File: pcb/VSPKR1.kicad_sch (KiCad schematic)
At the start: 17 parts, among them J1 USB_C_Receptacle_USB2.0_14P, SW1 RESET, SW2 BOOT, U1 ESP32-S3-WROOM-1, U2 AMS1117-3.3

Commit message: added speaker stuffs
but i havent actually connected it to esp32
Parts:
- added C10, C7: 0.1uF, symbol Device:C
- added C6, C9: 2.2uF, symbol Device:C
- added C8: 1uF, symbol Device:C
- added R7: 1K, symbol Device:R
- added R8: 10K, symbol Device:R
- added SW3: SW_SPDT, symbol Switch:SW_SPDT
- added U3: PCM5102A, Package_SO:TSSOP-20_4.4x6.5mm_P0.65mm, symbol Audio:PCM5102A
- added U4: PAM8403D, Package_SO:SOIC-16_3.9x9.9mm_P1.27mm, symbol Amplifier_Audio:PAM8403D
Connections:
- net +3V3: now also C7.2, SW3.3 (C), U3.1 (CPVDD), U3.17 (XSMT), U3.20 (DVDD), U3.8 (AVDD)
- net +5V: now also U4.13 (PVDD), U4.4 (PVDD), U4.6 (VDD)
- net GND: now also C10.2, C9.2, R8.2, SW3.1 (A), U3.10 (DEMP), U3.11 (FLT), U3.12 (SCK), U3.16 (FMT), U3.19 (DGND), U3.3 (CPGND), U3.9 (AGND), U4.11 (GND), U4.15 (PGND), U4.2 (PGND)
- net SCK: no longer U1.15 (IO3)
- net WS: now also U3.15 (LRCK)
- net DOUT: now reaches U1.4 (IO4)
- net DOUT: now also U3.14 (DIN)
- net at U1.5 (IO5): now also R7.2
- new net: C10.1, U4.8 (VREF)
- new net: SW3.2 (B), U4.5 (~{MUTE})
- new net: C8.1, U3.18 (LDOO)
- new net: C6.1, U3.2 (CAPP)
- new net: C6.2, U3.4 (CAPM)
- new net: C7.1, U3.5 (VNEG)
- new net: C8.2, C9.1
- new net BCK: U1.15 (IO3), U3.13 (BCK)
- new net LEFT-CHANNEL-OUT: U3.6 (OUTL), U4.7 (INL)
- new net RIGHT-CHANNEL-OUT: U3.7 (OUTR), U4.10 (INR)
- new net SHND: R7.1, R8.1, U4.12 (~{SHDN})
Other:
- note added: "5V -> 3.3V Step Down"
- note added: "Mic"
- note added: "Microphone! No data collection here."
- note added: "Power Source"
- note added: "Sound"
- note removed: "Mic / Sound"
- moved on the sheet: C1, C2, J1, R1, R2, U2

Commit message: pcb time!!111!!!!1!
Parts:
- removed SW3: SW_SPDT, symbol Switch:SW_SPDT
- added C11: 22uF, Capacitor_SMD:C_0805_2012Metric_Pad1.18x1.45mm_HandSolder, symbol Device:C
- added C12: 100nF, Capacitor_SMD:C_0805_2012Metric_Pad1.18x1.45mm_HandSolder, symbol Device:C
- added J2, J3: Screw_Terminal_01x02, TerminalBlock_Phoenix:TerminalBlock_Phoenix_MKDS-1,5-2_1x02_P5.00mm_Horizontal, symbol Connector:Screw_Terminal_01x02
- C1, C10, C2, C3, C4, C5, C6, C7, C8, C9: footprint (none) -> Capacitor_SMD:C_0805_2012Metric_Pad1.18x1.45mm_HandSolder
- J1: footprint (none) -> Connector_USB:USB_C_Receptacle_GCT_USB4105-xx-A_16P_TopMnt_Horizontal
- R1, R2, R3, R4, R5, R6, R7, R8: footprint (none) -> Resistor_SMD:R_0805_2012Metric_Pad1.20x1.40mm_HandSolder
- SW1, SW2: footprint (none) -> Button_Switch_SMD:SW_Push_1P1T_NO_CK_PTS125Sx43SMTR
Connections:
- net +3V3: now also U4.5 (~{MUTE}), C11.1, C12.1
- net GND: now also C1.2, C2.2, C11.2, C12.2
- net at U4.1 (LOUT+): now also J2.2 (Pin_2)
- net at U4.14 (ROUT-): now also J3.2 (Pin_2)
- net at U4.16 (ROUT+): now also J3.1 (Pin_1)
- net at U4.3 (LOUT-): now also J2.1 (Pin_1)
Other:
- note added: "LSPEAKER Out"
- note added: "Left Speaker"
- note added: "RSPEAKER Out"
- note added: "Right Speaker"
- moved on the sheet: MK1, R6

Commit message: pcb
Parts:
- added H1, H2, H3, H4: MountingHole, MountingHole:MountingHole_2.2mm_M2, symbol Mechanical:MountingHole
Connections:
- net +3V3: no longer C7.2
- net GND: now also C5.2, C7.2, C8.2
- net at C8.1, U3.18 (LDOO): now also C9.1
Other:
- note added: "These are mounting holes for the PCB so it can be screwed down securely to the 3D printed case"
- moved on the sheet: C10, C6, C7, C8, C9, J2, J3, MK1, R6, R8, U3, U4

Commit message: git push -m "hmm"
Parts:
- added C13: 0.1uF, Capacitor_SMD:C_0805_2012Metric_Pad1.18x1.45mm_HandSolder, symbol Device:C
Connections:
- net +3V3: now also C13.1
- net GND: now also C13.2
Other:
- note added: "Keep Close!"
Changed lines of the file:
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@@
 		)
 	)
+	(text "Keep Close!"
+		(exclude_from_sim no)
+		(at 29.21 48.514 0)
+		(effects
+			(font
+				(size 0.762 0.762)
+			)
+		)
+	)
 	(text "Power Source\n"
 		(exclude_from_sim no)
@@
 		)
 	)
+	(text "Keep Close!"
+		(exclude_from_sim no)
+		(at 70.104 129.794 0)
+		(effects
+			(font
+				(size 0.762 0.762)
+			)
+		)
+	)
 	(text "Strapping (Don't use!)\n"
 		(exclude_from_sim no)
@@
 		)
 	)
+	(text "Keep Close!"
+		(exclude_from_sim no)
+		(at 89.662 89.154 0)
+		(effects
+			(font
+				(size 0.762 0.762)
+			)
+		)
+	)
 	(text "Power Management"
 		(exclude_from_sim no)
@@
 	)
 	(junction
+		(at 69.85 118.11)
+		(diameter 0)
+		(color 0 0 0 0)
+	)
+	(junction
 		(at 90.17 143.51)
 		(diameter 0)
@@
 	)
 	(junction
+		(at 69.85 140.97)
+		(diameter 0)
+		(color 0 0 0 0)
+	)
+	(junction
 		(at 36.83 125.73)
 		(diameter 0)
@@
 	(wire
 		(pts
+			(xy 69.85 140.97) (xy 71.12 140.97)
+		)
+		(stroke
+			(width 0)
+			(type default)
+		)
+	)
+	(wire
+		(pts
 			(xy 31.75 133.35) (xy 38.1 133.35)
 		)
@@
 	(wire
 		(pts
+			(xy 69.85 133.35) (xy 69.85 140.97)
+		)
+		(stroke
+			(width 0)
+			(type default)
+		)
+	)
+	(wire
+		(pts
 			(xy 162.56 50.8) (xy 165.1 50.8)
 		)
@@
 	(wire
 		(pts
+			(xy 69.85 118.11) (xy 71.12 118.11)
+		)
+		(stroke
+			(width 0)
+			(type default)
+		)
+	)
+	(wire
+		(pts
 			(xy 162.56 54.61) (xy 163.83 54.61)
 		)
@@
 	(wire
 		(pts
+			(xy 69.85 118.11) (xy 69.85 125.73)
+		)
+		(stroke
+			(width 0)
+			(type default)
+		)
+	)
+	(wire
+		(pts
 			(xy 148.59 64.77) (xy 148.59 63.5)
 		)
@@
 	(symbol
 		(lib_id "power:GND")
-		(at 69.85 140.97 90)
+		(at 71.12 140.97 90)
 		(unit 1)
 		(body_style 1)
@@
 		(dnp no)
 		(property "Reference" "#PWR09"
-			(at 76.2 140.97 0)
+			(at 77.47 140.97 0)
 			(hide yes)
 			(show_name no)
@@
 		)
 		(property "Value" "GND"
-			(at 72.39 140.97 90)
+			(at 73.66 140.97 90)
 			(show_name no)
 			(do_not_autoplace no)
@@
 		)
 		(property "Footprint" ""
-			(at 69.85 140.97 0)
+			(at 71.12 140.97 0)
 			(hide yes)
 			(show_name no)
@@
 		)
 		(property "Datasheet" ""
-			(at 69.85 140.97 0)
+			(at 71.12 140.97 0)
 			(hide yes)
 			(show_name no)
@@
 		)
 		(property "Description" "Power symbol creates a global label with name \"GND\" , ground"
-			(at 69.85 140.97 0)
+			(at 71.12 140.97 0)
 			(hide yes)
 			(show_name no)
@@
 	)
 	(symbol
+		(lib_id "Device:C")
+		(at 69.85 129.54 0)
+		(unit 1)
+		(body_style 1)
+		(exclude_from_sim no)
+		(in_bom yes)
+		(on_board yes)
+		(in_pos_files yes)
+		(dnp no)
+		(property "Reference" "C13"
+			(at 69.85 127.762 0)
+			(show_name no)
+			(do_not_autoplace no)
+			(effects
+				(font
+					(size 1.27 1.27)
+				)
+				(justify left)
+			)
+		)
+		(property "Value" "0.1uF"
+			(at 69.85 131.572 0)
+			(show_name no)
+			(do_not_autoplace no)
+			(effects
+				(font
+					(size 1.27 1.27)
+				)
+				(justify left)
+			)
+		)
+		(property "Footprint" "Capacitor_SMD:C_0805_2012Metric_Pad1.18x1.45mm_HandSolder"
+			(at 70.8152 133.35 0)
+			(hide yes)
+			(show_name no)
+			(do_not_autoplace no)
+			(effects
+				(font
+					(size 1.27 1.27)
+				)
+			)
+		)
+		(property "Datasheet" ""
+			(at 69.85 129.54 0)
+			(hide yes)
+			(show_name no)
+			(do_not_autoplace no)
+			(effects
+				(font
+					(size 1.27 1.27)
+				)
+			)
+		)
+		(property "Description" "Unpolarized capacitor"
+			(at 69.85 129.54 0)
+			(hide yes)
+			(show_name no)
+			(do_not_autoplace no)
+			(effects
+				(font
+					(size 1.27 1.27)
+				)
+			)
+		)
+		(pin "2"
+		)
+		(pin "1"
+		)
+		(instances
+			(project "VSPKR1"
+				(path "/2e4f9796-824b-4b67-bb2e-3853f897fb99"
+					(reference "C13")
+					(unit 1)
+				)
+			)
+		)
+	)
+	(symbol
 		(lib_id "Switch:SW_Push")
 		(at 97.79 139.7 0)
@@
 	(symbol
 		(lib_id "power:+3V3")
-		(at 69.85 118.11 270)
+		(at 71.12 118.11 270)
 		(unit 1)
 		(body_style 1)
@@
 		(dnp no)
 		(property "Reference" "#PWR011"
-			(at 66.04 118.11 0)
+			(at 67.31 118.11 0)
 			(hide yes)
 			(show_name no)
@@
 		)
 		(property "Value" "+3V3"
-			(at 72.39 117.856 90)
+			(at 73.66 117.856 90)
 			(show_name no)
 			(do_not_autoplace no)
@@
 		)
 		(property "Footprint" ""
-			(at 69.85 118.11 0)
+			(at 71.12 118.11 0)
 			(hide yes)
 			(show_name no)
@@
 		)
 		(property "Datasheet" ""
-			(at 69.85 118.11 0)
+			(at 71.12 118.11 0)
 			(hide yes)
 			(show_name no)
@@
 		)
 		(property "Description" "Power symbol creates a global label with name \"+3V3\""
-			(at 69.85 118.11 0)
+			(at 71.12 118.11 0)
 			(hide yes)
 			(show_name no)

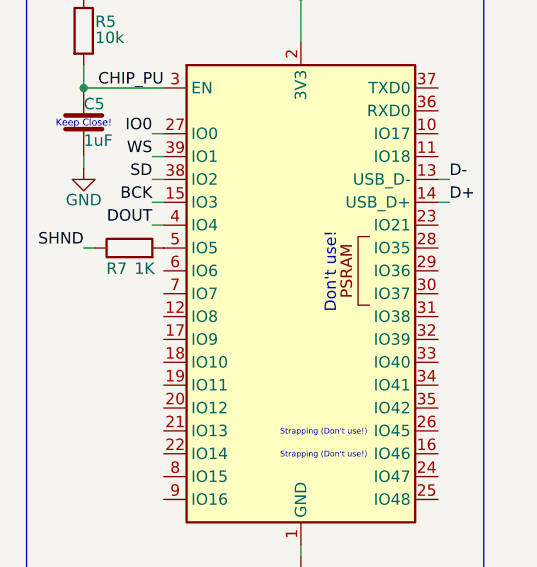
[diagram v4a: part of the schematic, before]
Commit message: Finished  the PCB
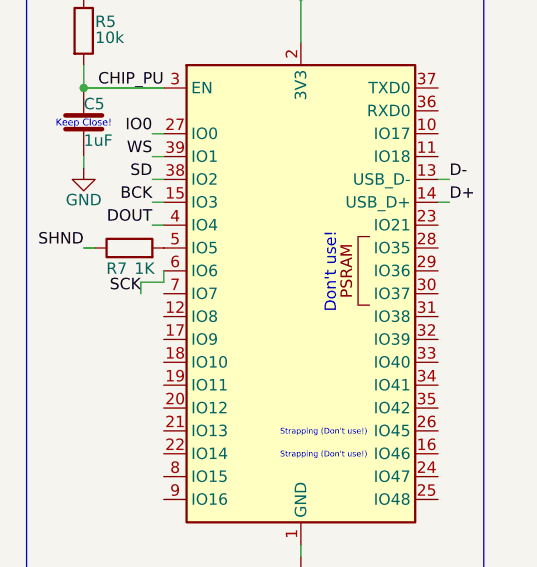
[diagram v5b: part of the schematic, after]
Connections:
- net SCK: now also U1.6 (IO6)
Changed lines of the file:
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@@
+	(wire
+		(pts
+			(xy 38.1 64.77) (xy 38.1 66.04)
+		)
+		(stroke
+			(width 0)
+			(type default)
+		)
+	)
 	(wire
 		(pts
@@
 	(wire
 		(pts
+			(xy 38.1 66.04) (xy 35.56 66.04)
+		)
+		(stroke
+			(width 0)
+			(type default)
+		)
+	)
+	(wire
+		(pts
 			(xy 161.29 83.82) (xy 162.56 83.82)
 		)
@@
 		(pts
 			(xy 92.71 116.84) (xy 90.17 116.84)
+		)
+		(stroke
+			(width 0)
+			(type default)
+		)
+	)
+	(wire
+		(pts
+			(xy 35.56 66.04) (xy 35.56 67.31)
 		)
 		(stroke
@@
 		)
 	)
+	(label "SCK"
+		(at 35.56 67.31 180)
+		(effects
+			(font
+				(size 1.27 1.27)
+			)
+			(justify right bottom)
+		)
+	)
